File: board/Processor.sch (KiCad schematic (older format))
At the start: 27 parts, among them Q3 2N7002DW, Q4 DMN65D8L-7, SW1 B3U-1000P-B, SW2 B3U-1000P-B, U1 TM4C123GH6PM, X1 TXC-7C

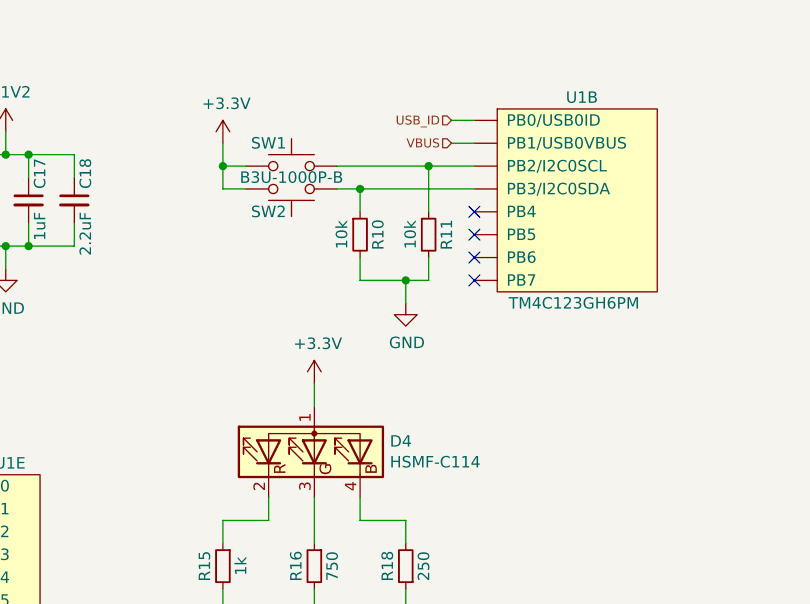
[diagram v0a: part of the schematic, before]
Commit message: Added a SPI present signal for the external bus to the CPU to make detection easier
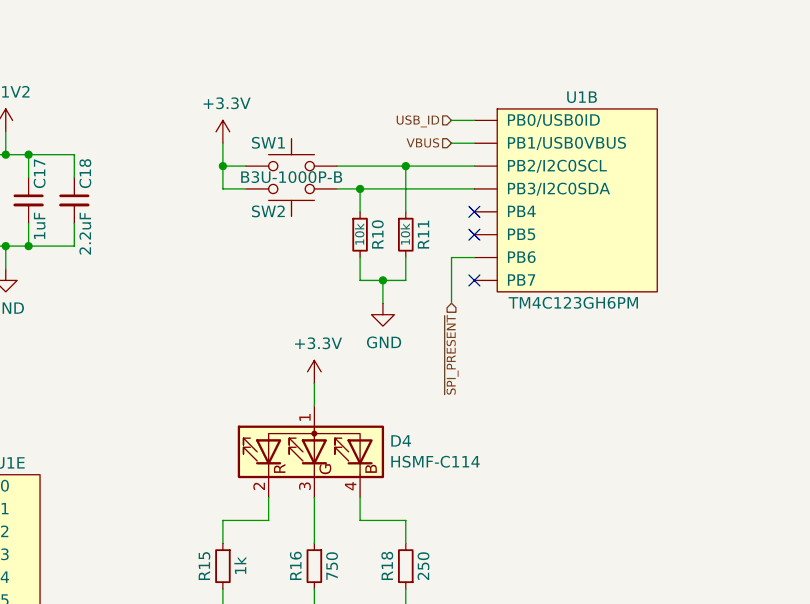
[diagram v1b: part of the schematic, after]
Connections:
- net ~SPI_PRESENT: now reaches U1.1 (PB6)
- no-connect marks 26 -> 25
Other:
- moved on the sheet: R11
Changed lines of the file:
@@
 NoConn ~ 5050 4050
 NoConn ~ 5050 4150
-NoConn ~ 5050 4250
 NoConn ~ 5050 4350
 Wire Wire Line
@@
 	4450 3950 4550 3950
 Wire Wire Line
-	4450 3850 4850 3850
+	4450 3850 4750 3850
 $Comp
 L Device:R_Small R10
@@
 P 4550 4150
 F 0 "R10" V 4600 4150 50  0000 C TNN
-F 1 "10k" V 4500 4150 50  0000 C BNN
+F 1 "10k" V 4550 4150 39  0000 C CNN
 F 2 "rhais_rcl:R0603" H 4550 4150 50  0001 C CNN
 F 3 "http://www.farnell.com/datasheets/1788326.pdf" H 4550 4150 50  0001 C CNN
@@
 L Device:R_Small R11
 U 1 1 5F94F5F1
-P 4850 4150
-F 0 "R11" V 4900 4150 50  0000 C TNN
-F 1 "10k" V 4800 4150 50  0000 C BNN
-F 2 "rhais_rcl:R0603" H 4850 4150 50  0001 C CNN
-F 3 "http://www.farnell.com/datasheets/1788326.pdf" H 4850 4150 50  0001 C CNN
-F 4 "Multicomp" H 4850 4150 50  0001 C CNN "MFR"
-F 5 "MC0063W0603110K" H 4850 4150 50  0001 C CNN "MPN"
-F 6 "2130939" H 4850 4150 50  0001 C CNN "OC_FARNELL"
-F 7 "https://uk.farnell.com/multicomp/mc0063w0603110k/res-10k-1-0-063w-0603-thick-film/dp/2130939" H 4850 4150 50  0001 C CNN "URL_FARNELL"
-	1    4850 4150
+P 4750 4150
+F 0 "R11" V 4800 4150 50  0000 C TNN
+F 1 "10k" V 4750 4150 39  0000 C CNN
+F 2 "rhais_rcl:R0603" H 4750 4150 50  0001 C CNN
+F 3 "http://www.farnell.com/datasheets/1788326.pdf" H 4750 4150 50  0001 C CNN
+F 4 "Multicomp" H 4750 4150 50  0001 C CNN "MFR"
+F 5 "MC0063W0603110K" H 4750 4150 50  0001 C CNN "MPN"
+F 6 "2130939" H 4750 4150 50  0001 C CNN "OC_FARNELL"
+F 7 "https://uk.farnell.com/multicomp/mc0063w0603110k/res-10k-1-0-063w-0603-thick-film/dp/2130939" H 4750 4150 50  0001 C CNN "URL_FARNELL"
+	1    4750 4150
 	1    0    0    -1
 $EndComp
@@
 	4550 3950 5050 3950
 Wire Wire Line
-	4850 3850 4850 4050
-Connection ~ 4850 3850
-Wire Wire Line
-	4850 3850 5050 3850
+	4750 3850 4750 4050
+Connection ~ 4750 3850
+Wire Wire Line
+	4750 3850 5050 3850
 $Comp
 L power:GND #PWR036
 U 1 1 5F954FA2
-P 4750 4450
-F 0 "#PWR036" H 4750 4200 50  0001 C CNN
-F 1 "GND" H 4755 4277 50  0000 C CNN
-F 2 "" H 4750 4450 50  0001 C CNN
-F 3 "" H 4750 4450 50  0001 C CNN
-	1    4750 4450
+P 4650 4450
+F 0 "#PWR036" H 4650 4200 50  0001 C CNN
+F 1 "GND" H 4655 4277 50  0000 C CNN
+F 2 "" H 4650 4450 50  0001 C CNN
+F 3 "" H 4650 4450 50  0001 C CNN
+	1    4650 4450
 	1    0    0    -1
 $EndComp
@@
 	4550 4250 4550 4350
 Wire Wire Line
-	4550 4350 4750 4350
-Wire Wire Line
-	4750 4350 4750 4450
-Wire Wire Line
-	4750 4350 4850 4350
-Wire Wire Line
-	4850 4350 4850 4250
-Connection ~ 4750 4350
+	4550 4350 4650 4350
+Wire Wire Line
+	4650 4350 4650 4450
+Wire Wire Line
+	4650 4350 4750 4350
+Wire Wire Line
+	4750 4350 4750 4250
+Connection ~ 4650 4350
 $Comp
 L power:+3.3V #PWR035
@@
 	1    0    0    -1
 $EndComp
+Text HLabel 4950 4450 3    39   Input ~ 0
+~SPI_PRESENT
+Wire Wire Line
+	5050 4250 4950 4250
+Wire Wire Line
+	4950 4250 4950 4450
 $EndSCHEMATC
